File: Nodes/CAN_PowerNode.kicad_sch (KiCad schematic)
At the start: 3 parts, among them IC3 TCAN1462VDRQ1

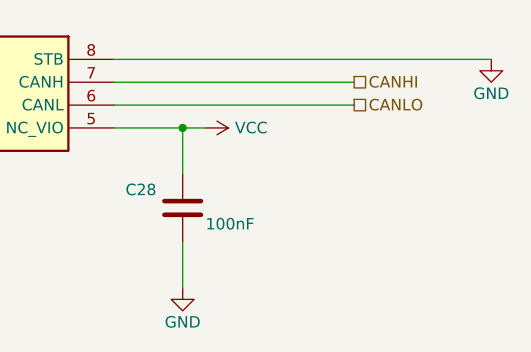
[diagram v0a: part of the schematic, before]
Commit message: Nodes v2.1.2 Improved
- Improved schematic design
- Added two 4.7 uF caps according to the datasheets of the microchips
- Other small changes
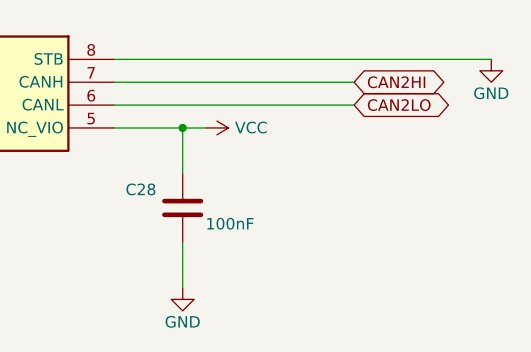
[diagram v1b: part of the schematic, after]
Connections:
- net CANHI renamed CAN2HI
- net CANLO renamed CAN2LO
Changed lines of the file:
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@@
 		)
 	)
-	(hierarchical_label "CANLO"
-		(shape passive)
+	(global_label "CAN2LO"
+		(shape bidirectional)
 		(at 185.42 92.71 0)
 		(fields_autoplaced yes)
@@
 			)
 			(justify left)
+		)
+		(property "Intersheetrefs" "${INTERSHEET_REFS}"
+			(at 196.7737 92.71 0)
+			(effects
+				(font
+					(size 1.27 1.27)
+				)
+				(justify left)
+				(hide yes)
+			)
+		)
+	)
+	(global_label "CAN2HI"
+		(shape bidirectional)
+		(at 185.42 90.17 0)
+		(fields_autoplaced yes)
+		(effects
+			(font
+				(size 1.27 1.27)
+			)
+			(justify left)
+		)
+		(property "Intersheetrefs" "${INTERSHEET_REFS}"
+			(at 196.3504 90.17 0)
+			(effects
+				(font
+					(size 1.27 1.27)
+				)
+				(justify left)
+				(hide yes)
+			)
 		)
 	)
@@
 		)
 	)
-	(hierarchical_label "CANHI"
-		(shape passive)
-		(at 185.42 90.17 0)
-		(fields_autoplaced yes)
-		(effects
-			(font
-				(size 1.27 1.27)
-			)
-			(justify left)
-		)
-	)

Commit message: Nodes v2.2
- This version not compatible with BOB v.2.1.2 and older!
- Completely new layout design
- New power supply system with new voltage regulators
- New microchip STM32G431RBTx for the Analog Node
- New connection system (instead of 18 pin headers now 8 pin and pins were grouped by functions)
- Reduced size of the board by 5%
- Removed power switch for the Analog Node (because this functionality is now provided by a separate voltage regulator. for a more stable voltage)
- Removable ground from the holes added
- Layer numbers added
- Small improvements of the components information were made
- New oscillator for the Nodes
- Removed CAN1, so now only one CAN connection due to the capabilities of the new microchip
- Other small changes and fixes on the schematic and design
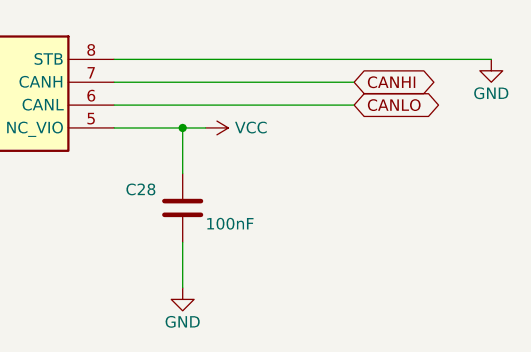
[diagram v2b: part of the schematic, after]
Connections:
- net CAN2HI renamed CANHI
- net CAN2LO renamed CANLO
